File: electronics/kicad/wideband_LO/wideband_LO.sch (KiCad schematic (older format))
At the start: 25 parts, among them U1 BFP620

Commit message: further fdtd
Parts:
- removed C2, C5: 10 pF, 0402, symbol SparkFun-Capacitors:6PF-0402-50V-0.5%
- added C? (x2): 10 pF, 0402, symbol SparkFun-Capacitors:6PF-0402-50V-0.5%
- C4: Spice_Lib_File (none) -> /home/arthurdent/Projects/covidinator/electronics/models/10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; Spice_Model (none) -> 10pf0402; Spice_Netlist_Enabled (none) -> Y; Spice_Primitive (none) -> X
- D2: Spice_Lib_File (none) -> /home/arthurdent/Projects/covidinator/electronics/models/SM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; Spice_Model (none) -> SMV2019079LF; Spice_Netlist_Enabled (none) -> Y; Spice_Primitive (none) -> X
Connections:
- net at R2.2, U1.1 (B): now also C?.1
- net at C4.1, L3.2, U1.3 (C): now also C?.2
- net at D3.2 (A), R5.1: now also C?.1
- net at D2.2 (A), R4.2: now also C?.2
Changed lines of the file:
@@
 Wire Wire Line
 	3500 3050 3950 3050
-$Comp
-L SparkFun-Capacitors:6PF-0402-50V-0.5% C5
-U 1 1 5EE0CC0E
-P 4050 3050
-F 0 "C5" V 3816 3100 45  0000 C CNN
-F 1 "10 pF" V 3900 3100 45  0000 C CNN
-F 2 "0402" H 4050 3300 20  0001 C CNN
-F 3 "" H 4050 3050 50  0001 C CNN
-F 4 "" H 4158 3016 60  0000 L CNN "Field4"
-	1    4050 3050
-	0    1    1    0
-$EndComp
 Wire Wire Line
 	4850 3050 4750 3050
@@
 Wire Wire Line
 	3200 3250 3100 3250
-$Comp
-L SparkFun-Capacitors:6PF-0402-50V-0.5% C2
-U 1 1 5EE21BEE
-P 2650 3250
-F 0 "C2" V 2416 3300 45  0000 C CNN
-F 1 "10 pF" V 2500 3300 45  0000 C CNN
-F 2 "0402" H 2650 3500 20  0001 C CNN
-F 3 "" H 2650 3250 50  0001 C CNN
-F 4 "" H 2758 3216 60  0000 L CNN "Field4"
-	1    2650 3250
-	0    -1   -1   0
-$EndComp
 Wire Wire Line
 	1900 3250 2000 3250
-$Comp
-L SparkFun-Coils:INDUCTOR-0402-3.9NH L1
-U 1 1 5EE21BFD
-P 1400 3250
-F 0 "L1" V 1579 3250 45  0000 C CNN
-F 1 "1 nH" V 1495 3250 45  0000 C CNN
-F 2 "0402" H 1400 3500 20  0001 C CNN
-F 3 "" H 1400 3250 50  0001 C CNN
-F 4 "" H 1452 3166 60  0000 L CNN "Field4"
-	1    1400 3250
-	0    1    1    0
-$EndComp
-$Comp
-L power:GND #PWR0102
-U 1 1 5EE21C04
-P 1200 3250
-F 0 "#PWR0102" H 1200 3250 30  0001 C CNN
-F 1 "GND" H 1200 3180 30  0001 C CNN
-F 2 "" H 1200 3250 50  0001 C CNN
-F 3 "" H 1200 3250 50  0001 C CNN
-	1    1200 3250
-	0    1    1    0
-$EndComp
 $Comp
 L SparkFun-Resistors:RESISTOR0402 R1
@@
 F 3 "" H 3050 3050 50  0001 C CNN
 F 4 "" H 3158 3016 60  0000 L CNN "Field4"
+F 5 "X" H 3050 3050 50  0001 C CNN "Spice_Primitive"
+F 6 "10pf0402" H 3050 3050 50  0001 C CNN "Spice_Model"
+F 7 "Y" H 3050 3050 50  0001 C CNN "Spice_Netlist_Enabled"
+F 8 "/home/arthurdent/Projects/covidinator/electronics/models/10pf0402.lib" H 3050 3050 50  0001 C CNN "Spice_Lib_File"
 	1    3050 3050
 	0    1    1    0
@@
 F 2 "Diode_SMD:D_SOD-523" H 2250 3250 50  0001 C CNN
 F 3 "~" H 2250 3250 50  0001 C CNN
+F 4 "X" H 2250 3250 50  0001 C CNN "Spice_Primitive"
+F 5 "SMV2019079LF" H 2250 3250 50  0001 C CNN "Spice_Model"
+F 6 "Y" H 2250 3250 50  0001 C CNN "Spice_Netlist_Enabled"
+F 7 "/home/arthurdent/Projects/covidinator/electronics/models/SMV2019079LF.lib" H 2250 3250 50  0001 C CNN "Spice_Lib_File"
 	1    2250 3250
 	1    0    0    -1
@@
 Wire Wire Line
 	2400 3250 2450 3250
-Connection ~ 2450 3250
 $Comp
 L Device:D D3
@@
 Wire Wire Line
 	4350 3050 4250 3050
+$Comp
+L power:GND #PWR0102
+U 1 1 5EE21C04
+P 1200 3250
+F 0 "#PWR0102" H 1200 3250 30  0001 C CNN
+F 1 "GND" H 1200 3180 30  0001 C CNN
+F 2 "" H 1200 3250 50  0001 C CNN
+F 3 "" H 1200 3250 50  0001 C CNN
+	1    1200 3250
+	0    1    1    0
+$EndComp
+$Comp
+L SparkFun-Coils:INDUCTOR-0402-3.9NH L1
+U 1 1 5EE21BFD
+P 1400 3250
+F 0 "L1" V 1579 3250 45  0000 C CNN
+F 1 "1 nH" V 1495 3250 45  0000 C CNN
+F 2 "0402" H 1400 3500 20  0001 C CNN
+F 3 "" H 1400 3250 50  0001 C CNN
+F 4 "" H 1452 3166 60  0000 L CNN "Field4"
+	1    1400 3250
+	0    1    1    0
+$EndComp
+$Comp
+L SparkFun-Capacitors:6PF-0402-50V-0.5% C?
+U 1 1 5EEB34DA
+P 4050 3050
+F 0 "C?" V 3816 3100 45  0000 C CNN
+F 1 "10 pF" V 3900 3100 45  0000 C CNN
+F 2 "0402" H 4050 3300 20  0001 C CNN
+F 3 "" H 4050 3050 50  0001 C CNN
+F 4 "" H 4158 3016 60  0000 L CNN "Field4"
+F 5 "X" H 4050 3050 50  0001 C CNN "Spice_Primitive"
+F 6 "10pf0402" H 4050 3050 50  0001 C CNN "Spice_Model"
+F 7 "Y" H 4050 3050 50  0001 C CNN "Spice_Netlist_Enabled"
+F 8 "/home/arthurdent/Projects/covidinator/electronics/models/10pf0402.lib" H 4050 3050 50  0001 C CNN "Spice_Lib_File"
+	1    4050 3050
+	0    1    1    0
+$EndComp
 Connection ~ 4250 3050
+$Comp
+L SparkFun-Capacitors:6PF-0402-50V-0.5% C?
+U 1 1 5EEB3D3A
+P 2550 3250
+F 0 "C?" V 2316 3300 45  0000 C CNN
+F 1 "10 pF" V 2400 3300 45  0000 C CNN
+F 2 "0402" H 2550 3500 20  0001 C CNN
+F 3 "" H 2550 3250 50  0001 C CNN
+F 4 "" H 2658 3216 60  0000 L CNN "Field4"
+F 5 "X" H 2550 3250 50  0001 C CNN "Spice_Primitive"
+F 6 "10pf0402" H 2550 3250 50  0001 C CNN "Spice_Model"
+F 7 "Y" H 2550 3250 50  0001 C CNN "Spice_Netlist_Enabled"
+F 8 "/home/arthurdent/Projects/covidinator/electronics/models/10pf0402.lib" H 2550 3250 50  0001 C CNN "Spice_Lib_File"
+	1    2550 3250
+	0    1    1    0
+$EndComp
+Connection ~ 2450 3250
 $EndSCHEMATC

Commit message: LO progress
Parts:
- added R?: 50, 0402, symbol SparkFun-Resistors:RESISTOR0402
- added Vvaractor: Vvaractor, TestPoint:TestPoint_Pad_1.5x1.5mm, symbol Connector:Test_Point
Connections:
- net GND: now also R?.1
- net Vvaractor: now also Vvaractor.1
- net at C4.2, TP1.1: now also R?.2
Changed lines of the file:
@@
 $EndComp
 Connection ~ 2450 3250
+$Comp
+L Connector:Test_Point Vvaractor
+U 1 1 5EED7014
+P 2000 4400
+F 0 "Vvaractor" V 2195 4472 50  0000 C CNN
+F 1 "Vvaractor" V 2104 4472 50  0000 C CNN
+F 2 "TestPoint:TestPoint_Pad_1.5x1.5mm" H 2200 4400 50  0001 C CNN
+F 3 "~" H 2200 4400 50  0001 C CNN
+F 4 "I" H 2000 4400 50  0001 C CNN "Spice_Primitive"
+F 5 "dc 1" H 2000 4400 50  0001 C CNN "Spice_Model"
+F 6 "Y" H 2000 4400 50  0001 C CNN "Spice_Netlist_Enabled"
+	1    2000 4400
+	0    -1   -1   0
+$EndComp
+Connection ~ 2000 4400
+$Comp
+L SparkFun-Resistors:RESISTOR0402 R?
+U 1 1 5EED81DA
+P 2550 2850
+F 0 "R?" V 2455 2918 45  0000 L CNN
+F 1 "50" V 2539 2918 45  0000 L CNN
+F 2 "0402" H 2550 3000 20  0001 C CNN
+F 3 "" H 2550 2850 60  0001 C CNN
+F 4 " " V 2634 2918 60  0000 L CNN "Field4"
+	1    2550 2850
+	0    1    1    0
+$EndComp
+Connection ~ 2550 3050
+$Comp
+L power:GND #PWR?
+U 1 1 5EEDC0A6
+P 2550 2650
+F 0 "#PWR?" H 2550 2650 30  0001 C CNN
+F 1 "GND" H 2550 2580 30  0001 C CNN
+F 2 "" H 2550 2650 50  0001 C CNN
+F 3 "" H 2550 2650 50  0001 C CNN
+	1    2550 2650
+	-1   0    0    1
+$EndComp
 $EndSCHEMATC

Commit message: Board design ostensibly complete
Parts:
- D1, D3, D4: Spice_Lib_File (none) -> /home/arthurdent/Projects/covidinator/electronics/models/SM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; Spice_Model (none) -> SMV2019079LF; Spice_Netlist_Enabled (none) -> Y; Spice_Primitive (none) -> X
- U1: Spice_Node_Sequence (none) -> 3 1 2 4
- Vvaractor1: renamed from Vvaractor; Spice_Primitive I -> V
- gave numbers to parts that had none: 3
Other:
- moved on the sheet: C2

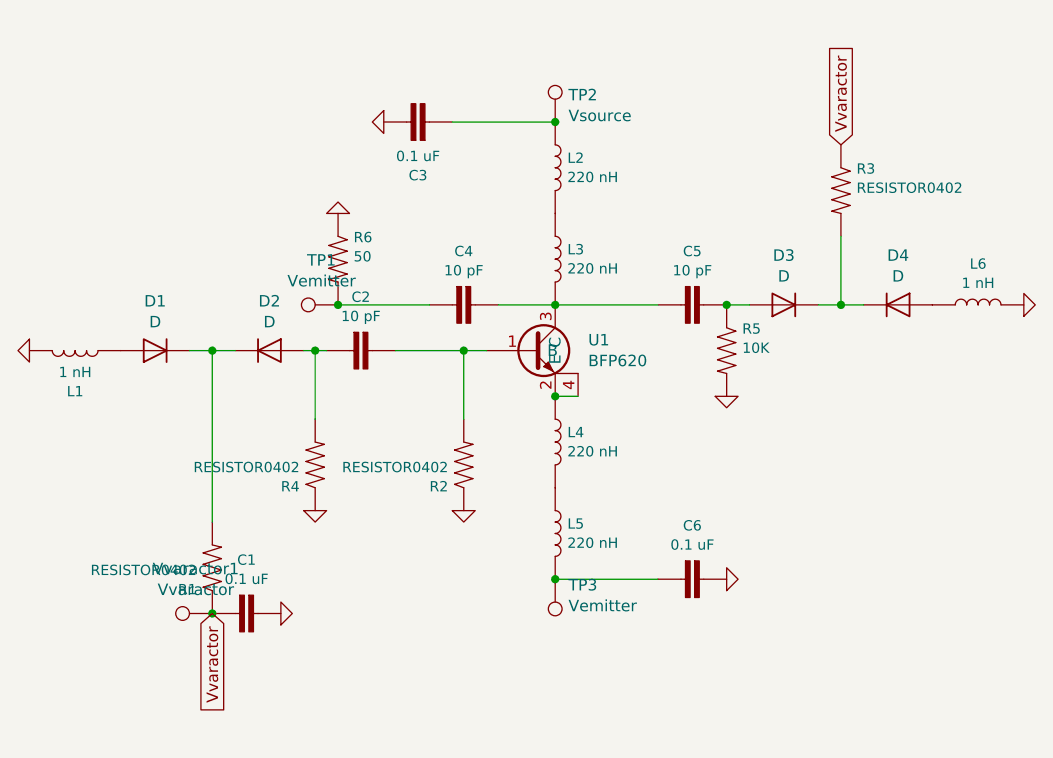
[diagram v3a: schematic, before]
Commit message: Removed a few otherwise ignored parameters from the diode model
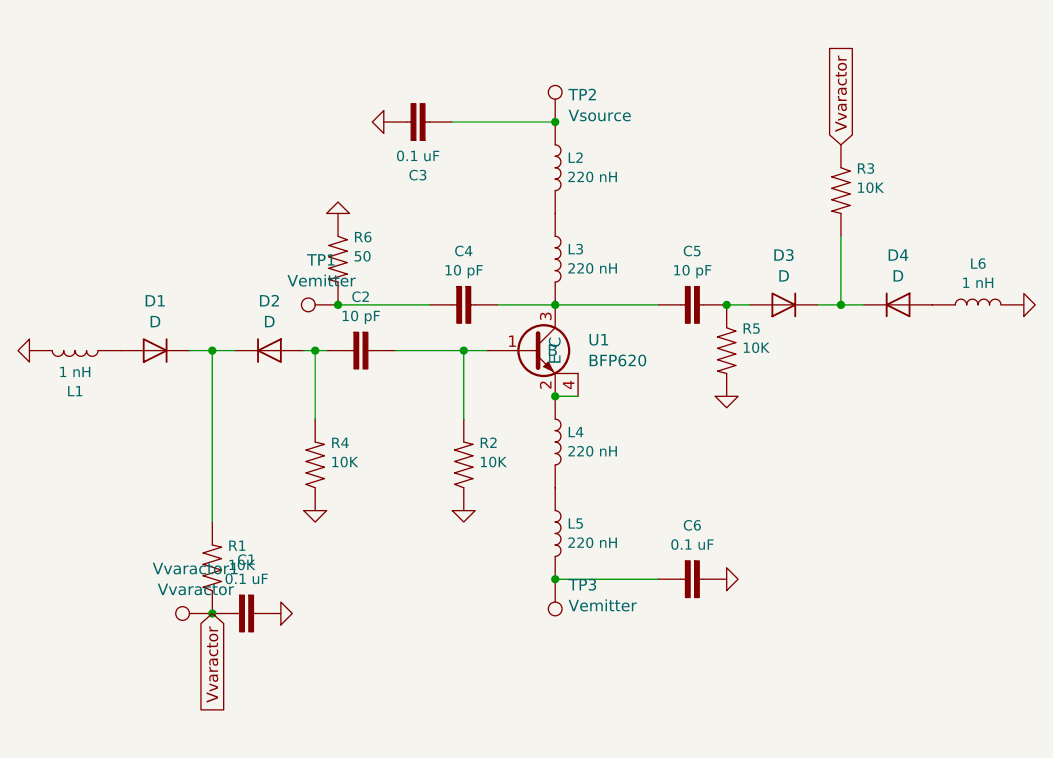
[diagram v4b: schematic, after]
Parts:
- R1, R2, R3, R4: value RESISTOR0402 -> 10K
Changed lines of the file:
@@
 P 4750 2550
 F 0 "R3" V 4655 2618 45  0000 L CNN
-F 1 "RESISTOR0402" V 4739 2618 45  0000 L CNN
+F 1 "10K" V 4739 2618 45  0000 L CNN
 F 2 "0402" H 4750 2700 20  0001 C CNN
 F 3 "" H 4750 2550 60  0001 C CNN
@@
 U 1 1 5EE21C0B
 P 2000 4200
-F 0 "R1" V 1905 4268 45  0000 L CNN
-F 1 "RESISTOR0402" V 1989 4268 45  0000 L CNN
+F 0 "R1" V 2095 4132 45  0000 R CNN
+F 1 "10K" V 2011 4132 45  0000 R CNN
 F 2 "0402" H 2000 4350 20  0001 C CNN
 F 3 "" H 2000 4200 60  0001 C CNN
-F 4 " " V 2084 4268 60  0000 L CNN "Field4"
+F 4 " " V 1916 4132 60  0000 R CNN "Field4"
 	1    2000 4200
 	0    -1   -1   0
@@
 U 1 1 5EE2D2F4
 P 3100 3750
-F 0 "R2" V 3005 3818 45  0000 L CNN
-F 1 "RESISTOR0402" V 3089 3818 45  0000 L CNN
+F 0 "R2" V 3195 3682 45  0000 R CNN
+F 1 "10K" V 3111 3682 45  0000 R CNN
 F 2 "0402" H 3100 3900 20  0001 C CNN
 F 3 "" H 3100 3750 60  0001 C CNN
-F 4 " " V 3184 3818 60  0000 L CNN "Field4"
+F 4 " " V 3016 3682 60  0000 R CNN "Field4"
 	1    3100 3750
 	0    -1   -1   0
@@
 U 1 1 5EE4E4E0
 P 2450 3750
-F 0 "R4" V 2355 3818 45  0000 L CNN
-F 1 "RESISTOR0402" V 2439 3818 45  0000 L CNN
+F 0 "R4" V 2545 3682 45  0000 R CNN
+F 1 "10K" V 2461 3682 45  0000 R CNN
 F 2 "0402" H 2450 3900 20  0001 C CNN
 F 3 "" H 2450 3750 60  0001 C CNN
-F 4 " " V 2534 3818 60  0000 L CNN "Field4"
+F 4 " " V 2366 3682 60  0000 R CNN "Field4"
 	1    2450 3750
 	0    -1   -1   0

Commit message: Sources are shorting.
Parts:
- TP1: Spice_Model (none) -> 0; Spice_Netlist_Enabled (none) -> N; Spice_Primitive (none) -> R
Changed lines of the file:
@@
 F 2 "TestPoint:TestPoint_Pad_1.5x1.5mm" H 2750 3050 50  0001 C CNN
 F 3 "~" H 2750 3050 50  0001 C CNN
+F 4 "R" H 2550 3050 50  0001 C CNN "Spice_Primitive"
+F 5 "0" H 2550 3050 50  0001 C CNN "Spice_Model"
+F 6 "N" H 2550 3050 50  0001 C CNN "Spice_Netlist_Enabled"
 	1    2550 3050
 	0    -1   -1   0

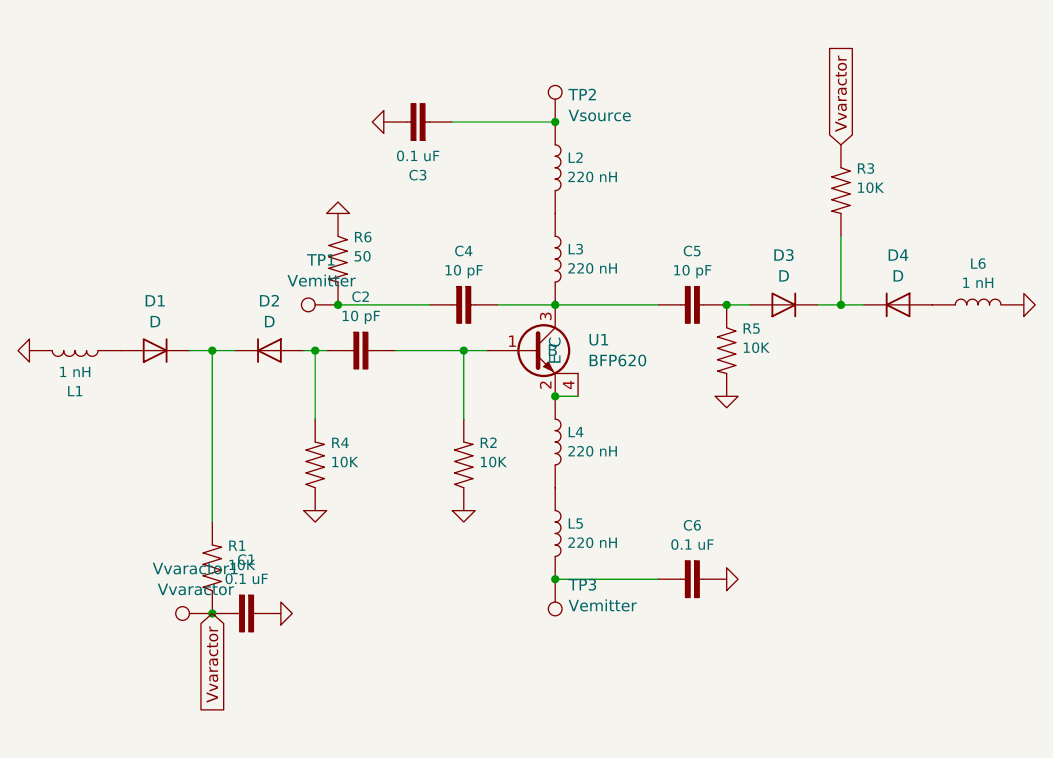
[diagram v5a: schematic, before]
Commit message: Sources still shorting
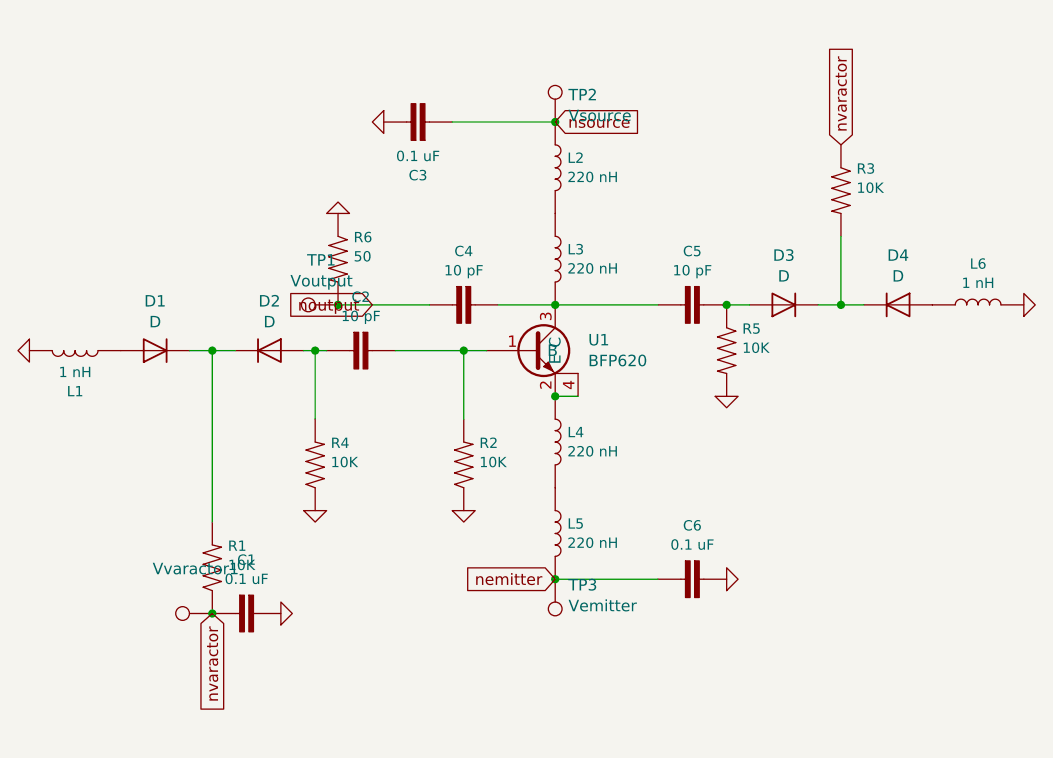
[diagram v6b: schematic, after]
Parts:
- TP1: value Vemitter -> Voutput; Spice_Model 0 -> 100M; Spice_Netlist_Enabled N -> Y
- Vvaractor1: value Vvaractor -> (none)
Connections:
- net nsource: now reaches C3.2, L2.1, TP2.1
- net nemitter: now reaches C6.2, L5.2, TP3.1
- net noutput: now reaches C4.2, R6.2, TP1.1
- net Vvaractor renamed nvaractor
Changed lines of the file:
@@
 P 2550 3050
 F 0 "TP1" V 2745 3122 50  0000 C CNN
-F 1 "Vemitter" V 2654 3122 50  0000 C CNN
+F 1 "Voutput" V 2654 3122 50  0000 C CNN
 F 2 "TestPoint:TestPoint_Pad_1.5x1.5mm" H 2750 3050 50  0001 C CNN
 F 3 "~" H 2750 3050 50  0001 C CNN
 F 4 "R" H 2550 3050 50  0001 C CNN "Spice_Primitive"
-F 5 "0" H 2550 3050 50  0001 C CNN "Spice_Model"
-F 6 "N" H 2550 3050 50  0001 C CNN "Spice_Netlist_Enabled"
+F 5 "100M" H 2550 3050 50  0001 C CNN "Spice_Model"
+F 6 "Y" H 2550 3050 50  0001 C CNN "Spice_Netlist_Enabled"
 	1    2550 3050
 	0    -1   -1   0
 $EndComp
-Text GLabel 2000 4400 3    50   Input ~ 0
-Vvaractor
-Text GLabel 4750 2350 1    50   Input ~ 0
-Vvaractor
 $Comp
 L SparkFun-Capacitors:4.7UF0603 C1
@@
 P 2000 4400
 F 0 "Vvaractor1" V 2195 4472 50  0000 C CNN
-F 1 "Vvaractor" V 2104 4472 50  0000 C CNN
+F 1 " " V 2104 4472 50  0000 C CNN
 F 2 "TestPoint:TestPoint_Pad_1.5x1.5mm" H 2200 4400 50  0001 C CNN
 F 3 "~" H 2200 4400 50  0001 C CNN
@@
 	0    -1   -1   0
 $EndComp
-Connection ~ 2000 4400
 $Comp
 L SparkFun-Resistors:RESISTOR0402 R6
@@
 	2450 3250 2500 3250
 Connection ~ 2450 3250
+Text GLabel 3500 2250 2    50   Input ~ 0
+nsource
+Text GLabel 2700 3050 0    50   Input ~ 0
+noutput
+Text GLabel 3500 4250 0    50   Input ~ 0
+nemitter
+Connection ~ 2000 4400
+Text GLabel 2000 4400 3    50   Input ~ 0
+nvaractor
+Text GLabel 4750 2350 1    50   Input ~ 0
+nvaractor
 $EndSCHEMATC

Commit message: Sim runs: ports not rotated.
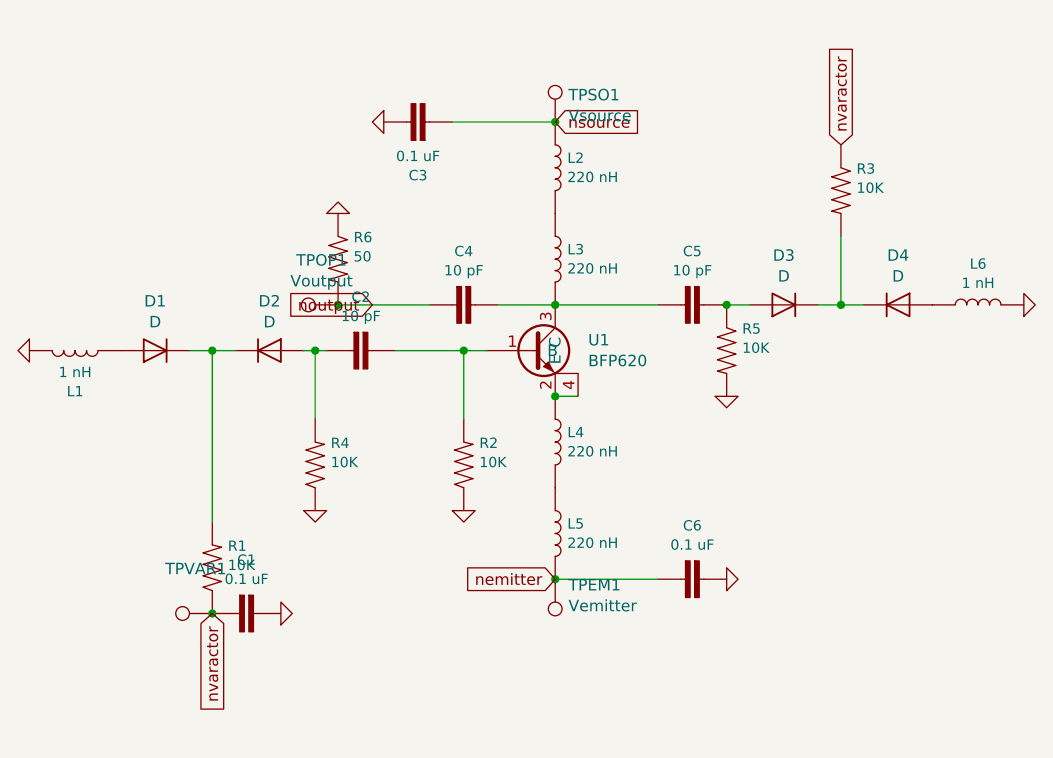
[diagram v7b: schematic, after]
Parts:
- TPEM1: renamed from TP3; Spice_Netlist_Enabled Y -> N
- TPOP1: renamed from TP1; Spice_Netlist_Enabled Y -> N
- TPSO1: renamed from TP2; Spice_Model pulse(0 2 20e-12 5e-12 1e-12 1 1) -> pulse(0 2 20p 5p 1p 1 1); Spice_Netlist_Enabled Y -> N
- renumbered Vvaractor1 to TPVAR1
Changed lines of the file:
@@
 $EndComp
 $Comp
-L Connector:Test_Point TP3
+L Connector:Test_Point TPEM1
 U 1 1 5EE3076A
 P 3500 4250
-F 0 "TP3" H 3442 4276 50  0000 R CNN
+F 0 "TPEM1" H 3442 4276 50  0000 R CNN
 F 1 "Vemitter" H 3442 4367 50  0000 R CNN
 F 2 "TestPoint:TestPoint_Pad_2.0x2.0mm" H 3700 4250 50  0001 C CNN
@@
 F 4 "V" H 3500 4250 50  0001 C CNN "Spice_Primitive"
 F 5 "dc -2" H 3500 4250 50  0001 C CNN "Spice_Model"
-F 6 "Y" H 3500 4250 50  0001 C CNN "Spice_Netlist_Enabled"
+F 6 "N" H 3500 4250 50  0001 C CNN "Spice_Netlist_Enabled"
 	1    3500 4250
 	-1   0    0    1
@@
 Connection ~ 3500 4250
 $Comp
-L Connector:Test_Point TP1
+L Connector:Test_Point TPOP1
 U 1 1 5EE35A86
 P 2550 3050
-F 0 "TP1" V 2745 3122 50  0000 C CNN
+F 0 "TPOP1" V 2745 3122 50  0000 C CNN
 F 1 "Voutput" V 2654 3122 50  0000 C CNN
 F 2 "TestPoint:TestPoint_Pad_1.5x1.5mm" H 2750 3050 50  0001 C CNN
@@
 F 4 "R" H 2550 3050 50  0001 C CNN "Spice_Primitive"
 F 5 "100M" H 2550 3050 50  0001 C CNN "Spice_Model"
-F 6 "Y" H 2550 3050 50  0001 C CNN "Spice_Netlist_Enabled"
+F 6 "N" H 2550 3050 50  0001 C CNN "Spice_Netlist_Enabled"
 	1    2550 3050
 	0    -1   -1   0
@@
 $EndComp
 $Comp
-L Connector:Test_Point Vvaractor1
+L Connector:Test_Point TPVAR1
 U 1 1 5EED7014
 P 2000 4400
-F 0 "Vvaractor1" V 2195 4472 50  0000 C CNN
+F 0 "TPVAR1" V 2195 4472 50  0000 C CNN
 F 1 " " V 2104 4472 50  0000 C CNN
 F 2 "TestPoint:TestPoint_Pad_1.5x1.5mm" H 2200 4400 50  0001 C CNN
@@
 $EndComp
 $Comp
-L Connector:Test_Point TP2
+L Connector:Test_Point TPSO1
 U 1 1 5EE45334
 P 3500 2250
-F 0 "TP2" H 3558 2368 50  0000 L CNN
+F 0 "TPSO1" H 3558 2368 50  0000 L CNN
 F 1 "Vsource" H 3558 2277 50  0000 L CNN
 F 2 "TestPoint:TestPoint_Pad_2.0x2.0mm" H 3700 2250 50  0001 C CNN
 F 3 "~" H 3700 2250 50  0001 C CNN
 F 4 "V" H 3500 2250 50  0001 C CNN "Spice_Primitive"
-F 5 "pulse(0 2 20e-12 5e-12 1e-12 1 1)" H 3500 2250 50  0001 C CNN "Spice_Model"
-F 6 "Y" H 3500 2250 50  0001 C CNN "Spice_Netlist_Enabled"
+F 5 "pulse(0 2 20p 5p 1p 1 1)" H 3500 2250 50  0001 C CNN "Spice_Model"
+F 6 "N" H 3500 2250 50  0001 C CNN "Spice_Netlist_Enabled"
 	1    3500 2250
 	1    0    0    -1

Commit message: More fixes
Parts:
- D1, D2, D3, D4: Spice_Node_Sequence (none) -> 2 1
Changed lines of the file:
@@
 F 6 "Y" H 2250 3250 50  0001 C CNN "Spice_Netlist_Enabled"
 F 7 "/home/arthurdent/Projects/covidinator/electronics/models/SMV2019079LF.lib" H 2250 3250 50  0001 C CNN "Spice_Lib_File"
+F 8 "2 1" H 2250 3250 50  0001 C CNN "Spice_Node_Sequence"
 	1    2250 3250
 	1    0    0    -1
@@
 F 6 "Y" H 5000 3050 50  0001 C CNN "Spice_Netlist_Enabled"
 F 7 "/home/arthurdent/Projects/covidinator/electronics/models/SMV2019079LF.lib" H 5000 3050 50  0001 C CNN "Spice_Lib_File"
+F 8 "2 1" H 5000 3050 50  0001 C CNN "Spice_Node_Sequence"
 	1    5000 3050
 	1    0    0    -1
@@
 F 6 "Y" H 1750 3250 50  0001 C CNN "Spice_Netlist_Enabled"
 F 7 "/home/arthurdent/Projects/covidinator/electronics/models/SMV2019079LF.lib" H 1750 3250 50  0001 C CNN "Spice_Lib_File"
+F 8 "2 1" H 1750 3250 50  0001 C CNN "Spice_Node_Sequence"
 	1    1750 3250
 	-1   0    0    1
@@
 F 6 "Y" H 4500 3050 50  0001 C CNN "Spice_Netlist_Enabled"
 F 7 "/home/arthurdent/Projects/covidinator/electronics/models/SMV2019079LF.lib" H 4500 3050 50  0001 C CNN "Spice_Lib_File"
+F 8 "2 1" H 4500 3050 50  0001 C CNN "Spice_Node_Sequence"
 	1    4500 3050
 	-1   0    0    1
